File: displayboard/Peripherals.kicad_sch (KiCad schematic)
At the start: 13 parts, among them IC1101 PCAL6416AHF, SW1101 Button 1, SW1102 Button 2, SW1103 Button 3, SW1104 Button 4

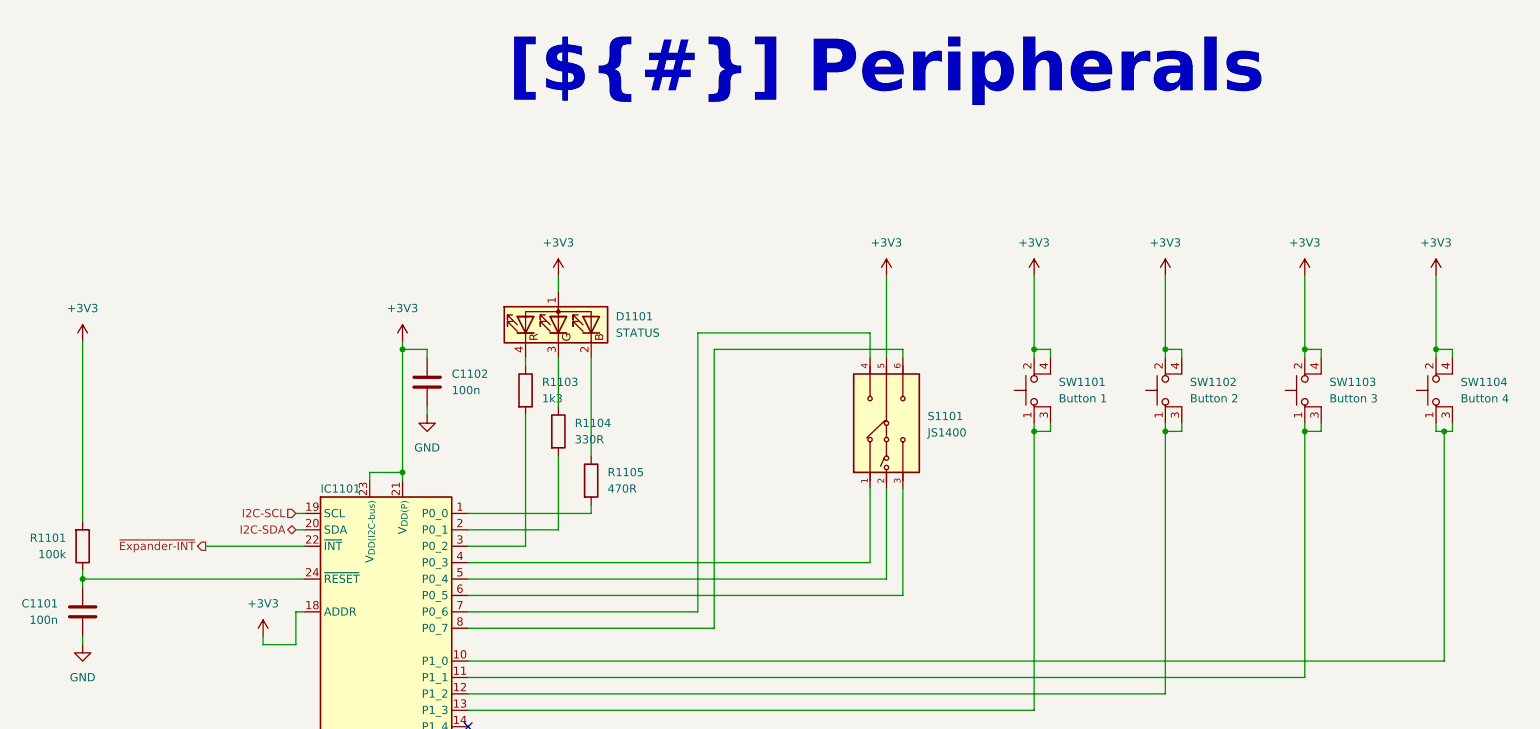
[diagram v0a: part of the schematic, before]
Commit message: Remove old production files, add cutout for the programming cable, add connector for mainboard cable
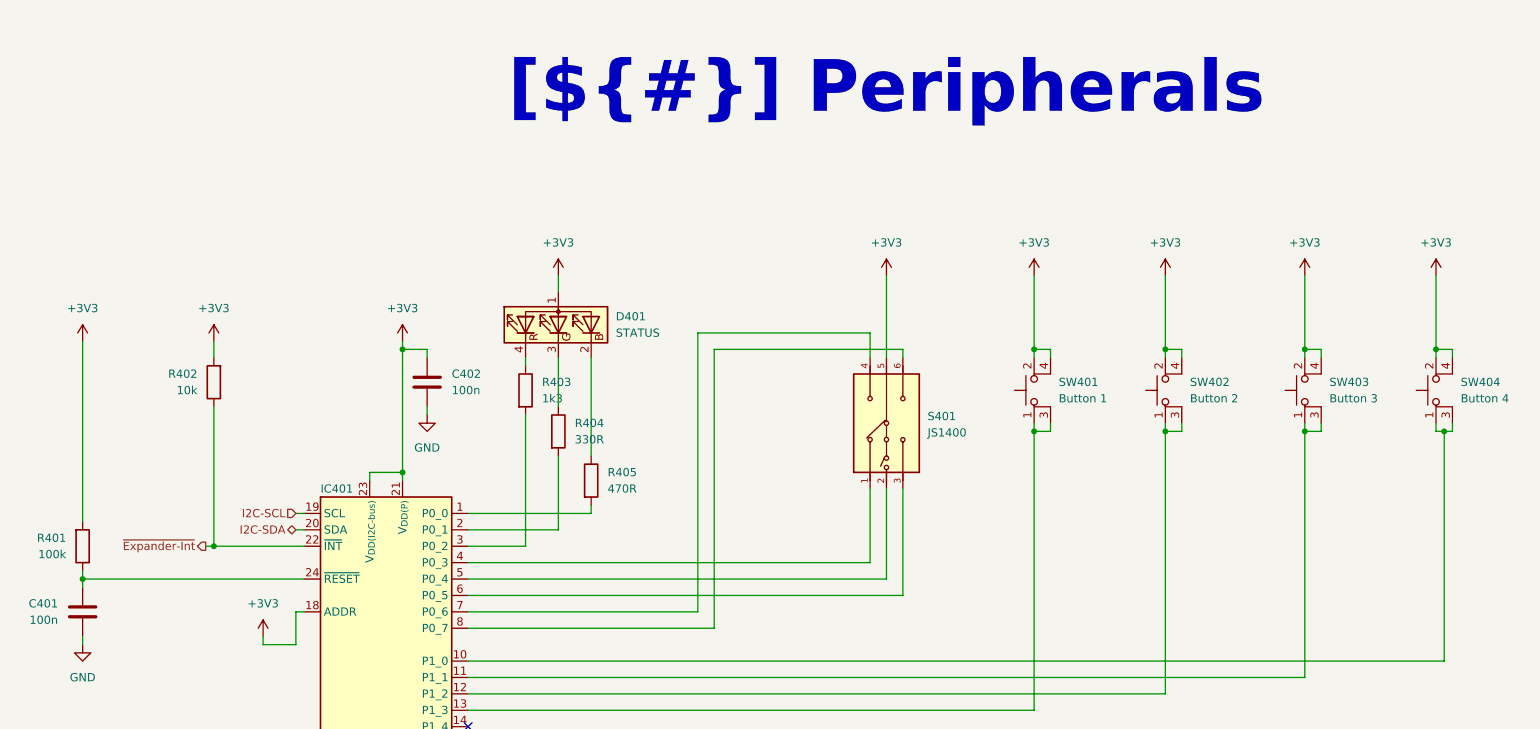
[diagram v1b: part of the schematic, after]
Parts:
- added R402: 10k, Resistor_SMD:R_0805_2012Metric, symbol Device:R
- renumbered C1101 to C401, C1102 to C402, D1101 to D401, IC1101 to IC401, R1101 to R401, R1103 to R403, R1104 to R404, R1105 to R405, S1101 to S401, SW1101 to SW401, SW1102 to SW402, SW1103 to SW403, SW1104 to SW404
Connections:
- net +3V3: now also R402.2
- net ~{Expander-INT} renamed ~{Expander-Int}
- net ~{Expander-Int}: now also R402.1

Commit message: Feature: Issue #19
- Replace JS1400BFQ with MU-BUE70R
- Add CI/CD workflow to check for changelog updates on PRs

Closes #19

Signed-off-by: Daniel Kampert <DanielKampert@kampis-elektroecke.de>
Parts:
- S401: value JS1400 -> NAVIGATION; footprint E-Switch:JS1400BVQ -> Apem:MU-BUE70R; symbol E-Switch:JS1400 -> Apem:MU; manf E-Switch -> Apem; manf# JS1400 -> MU-BUE70R; mouser# 612-JS1400 -> 642-MU-BUE70R
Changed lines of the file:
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@@
 	)
 	(symbol
-		(lib_id "E-Switch:JS1400")
+		(lib_id "Apem:MU")
 		(at 148.59 74.93 90)
 		(unit 1)
@@
 			)
 		)
-		(property "Value" "JS1400"
+		(property "Value" "NAVIGATION"
 			(at 154.94 76.4031 90)
 			(effects
@@
 			)
 		)
-		(property "Footprint" "E-Switch:JS1400BVQ"
+		(property "Footprint" "Apem:MU-BUE70R"
 			(at 235.89 48.26 0)
 			(effects
@@
 			)
 		)
-		(property "Datasheet" "https://configured-product-images.s3.amazonaws.com/2D/specs/JS1400BVQ.pdf"
+		(property "Datasheet" "https://www.apem.com/de/medias/download/PCB_MU_serie.pdf"
 			(at 335.89 48.26 0)
 			(effects
@@
 			)
 		)
-		(property "manf" "E-Switch"
+		(property "manf" "Apem"
 			(at 148.59 74.93 0)
 			(effects
@@
 			)
 		)
-		(property "manf#" "JS1400"
+		(property "manf#" "MU-BUE70R"
 			(at 148.59 74.93 0)
 			(effects
@@
 			)
 		)
-		(property "mouser#" "612-JS1400"
+		(property "mouser#" "642-MU-BUE70R"
 			(at 148.59 74.93 0)
 			(effects

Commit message: Added: Add a cutout for the display cable, add different assembly improvements
Signed-off-by: Daniel Kampert <DanielKampert@kampis-elektroecke.de>
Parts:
- D401: value STATUS -> Status
- S401: value NAVIGATION -> Navigation
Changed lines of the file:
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@@
 			)
 		)
-		(property "Value" "STATUS"
+		(property "Value" "Status"
 			(at 106.68 60.9599 90)
 			(effects
@@
 			)
 		)
-		(property "Value" "NAVIGATION"
+		(property "Value" "Navigation"
 			(at 154.94 76.4031 90)
 			(effects

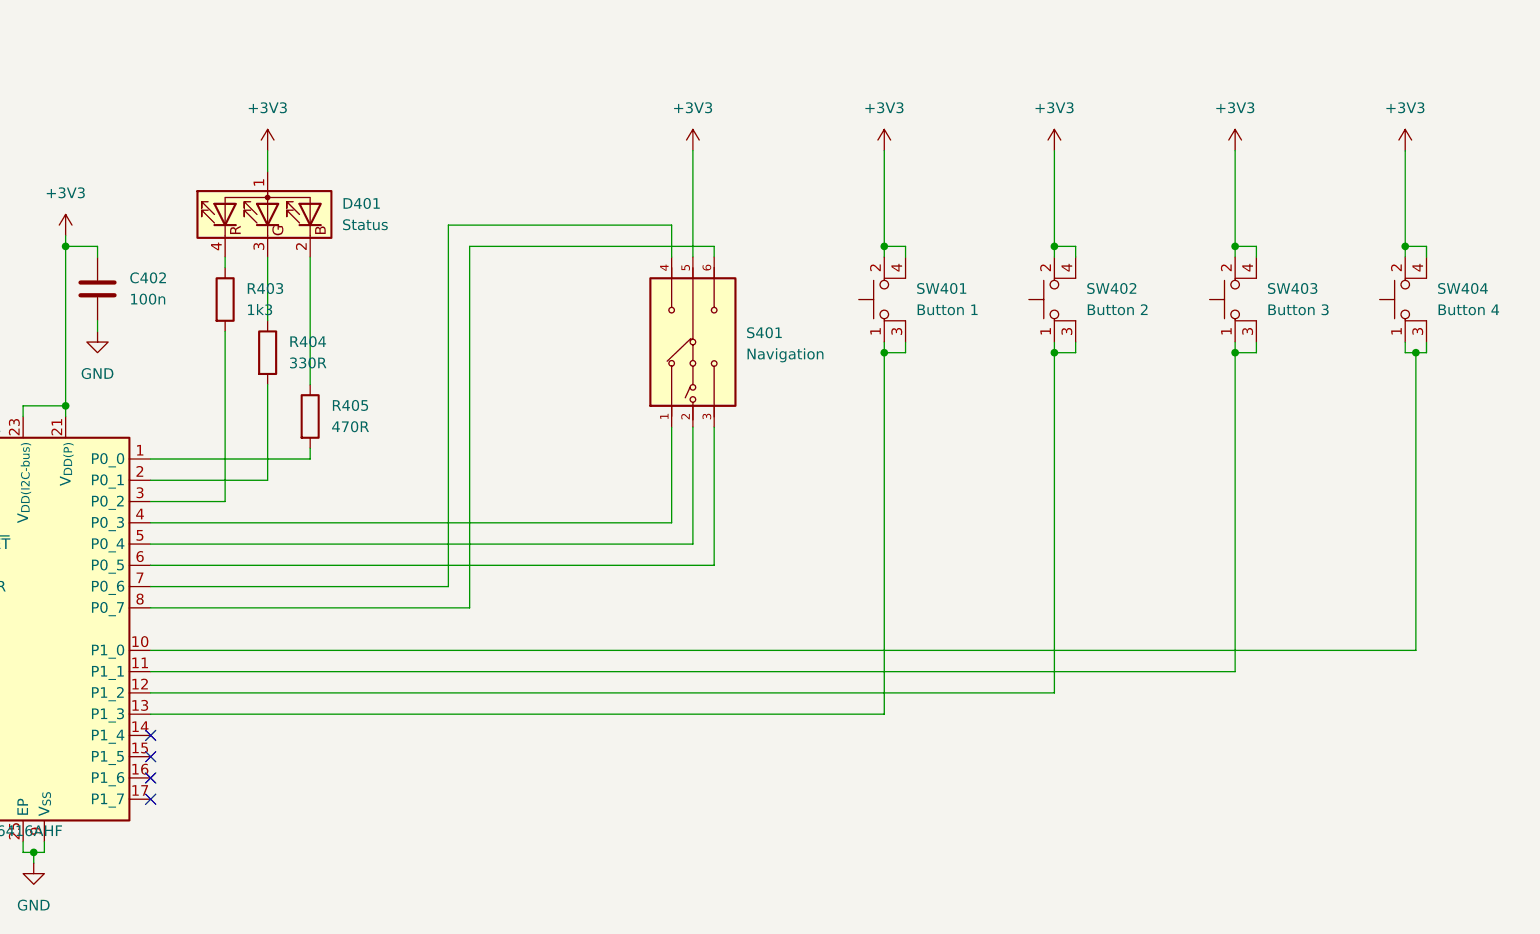
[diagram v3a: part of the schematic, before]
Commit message: Feature: Add debounce capacitors to push buttons
- Replace NPN transistor with N-Channel MOSFET

Signed-off-by: Daniel Kampert <DanielKampert@kampis-elektroecke.de>
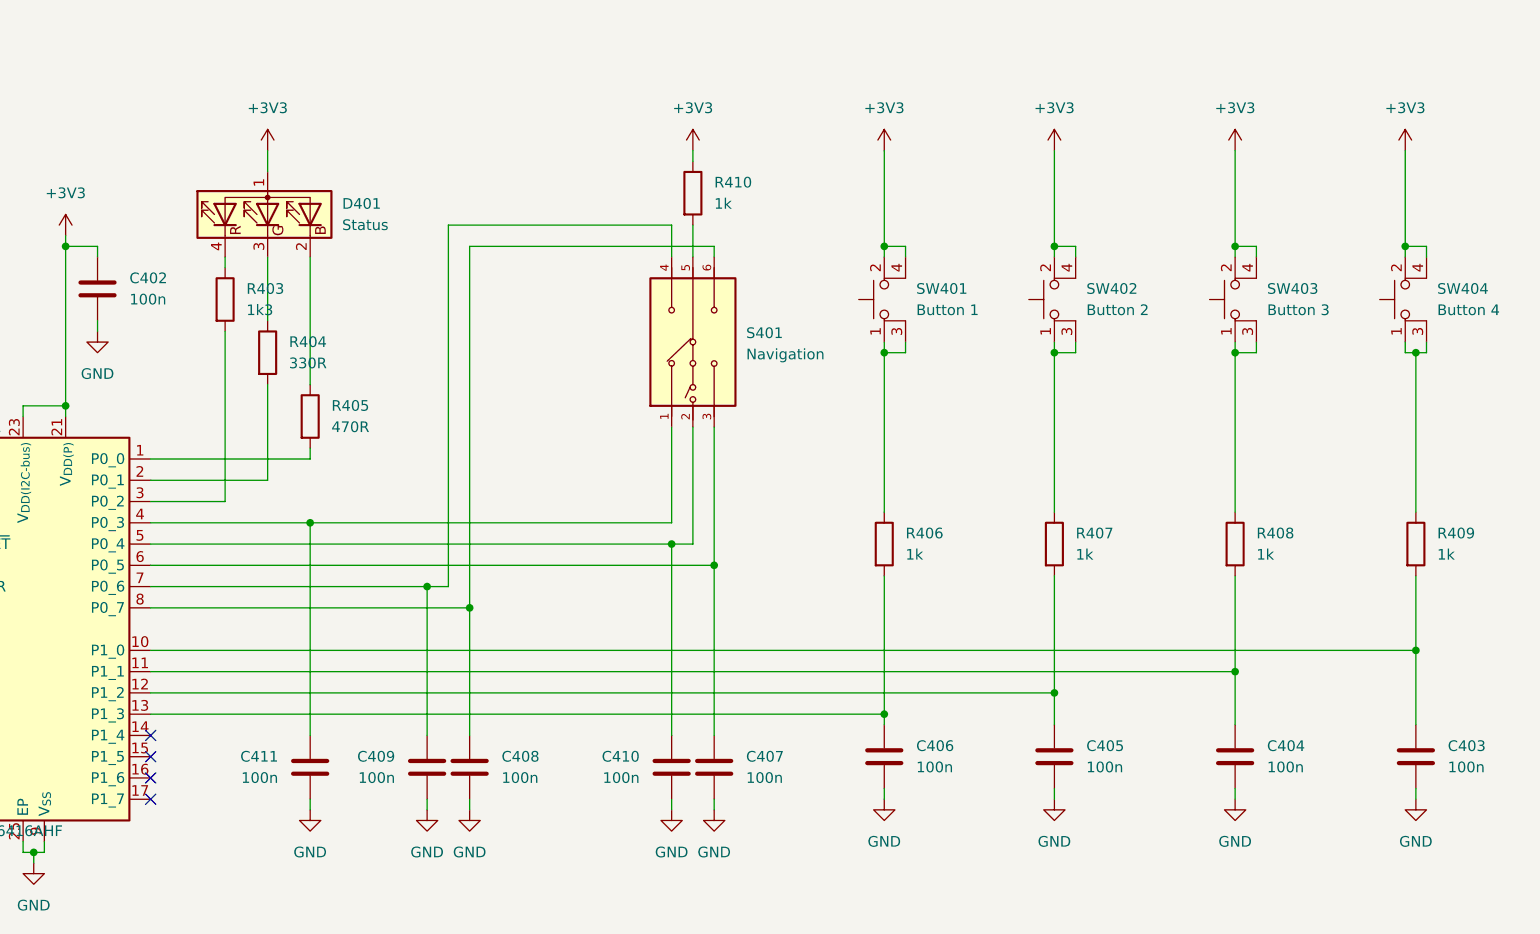
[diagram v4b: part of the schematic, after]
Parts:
- added C403, C404, C405, C406, C407, C408, C409, C410, C411: 100n, Capacitor_SMD:C_0805_2012Metric, symbol Device:C
- added R406, R407, R408, R409, R410: 1k, Resistor_SMD:R_0805_2012Metric, symbol Device:R
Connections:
- net +3V3: now also R410.1; no longer S401.5
- net GND: now also C403.2, C404.2, C405.2, C406.2, C407.2, C408.2, C409.2, C410.2, C411.2
- net at SW401.1, SW401.3: now also R406.1; no longer IC401.13 (P1_3)
- net at SW403.1, SW403.3: now also R408.1; no longer IC401.11 (P1_1)
- net at SW402.1, SW402.3: now also R407.1; no longer IC401.12 (P1_2)
- net at SW404.1, SW404.3: now also R409.1; no longer IC401.10 (P1_0)
- net at IC401.4 (P0_3), S401.1: now also C411.1
- net at IC401.5 (P0_4), S401.2: now also C410.1
- net at IC401.6 (P0_5), S401.3: now also C407.1
- net at IC401.7 (P0_6), S401.4: now also C409.1
- net at IC401.8 (P0_7), S401.6: now also C408.1
- new net: C406.1, IC401.13 (P1_3), R406.2
- new net: C403.1, IC401.10 (P1_0), R409.2
- new net: C405.1, IC401.12 (P1_2), R407.2
- new net: C404.1, IC401.11 (P1_1), R408.2
- new net: R410.2, S401.5

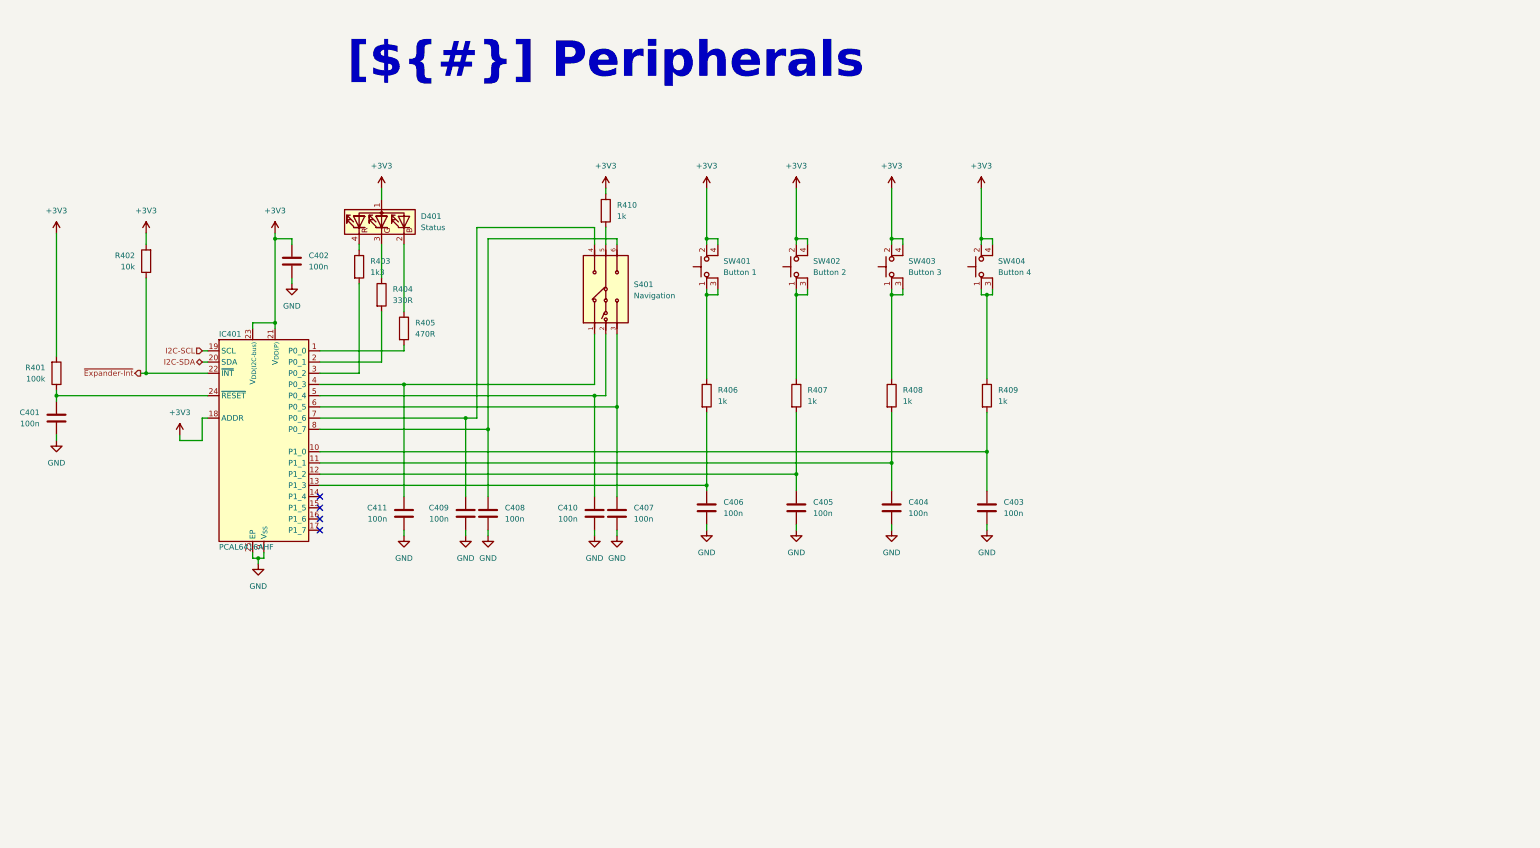
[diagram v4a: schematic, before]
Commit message: Changed: Rework debouncing logic
Signed-off-by: Daniel Kampert <DanielKampert@kampis-elektroecke.de>
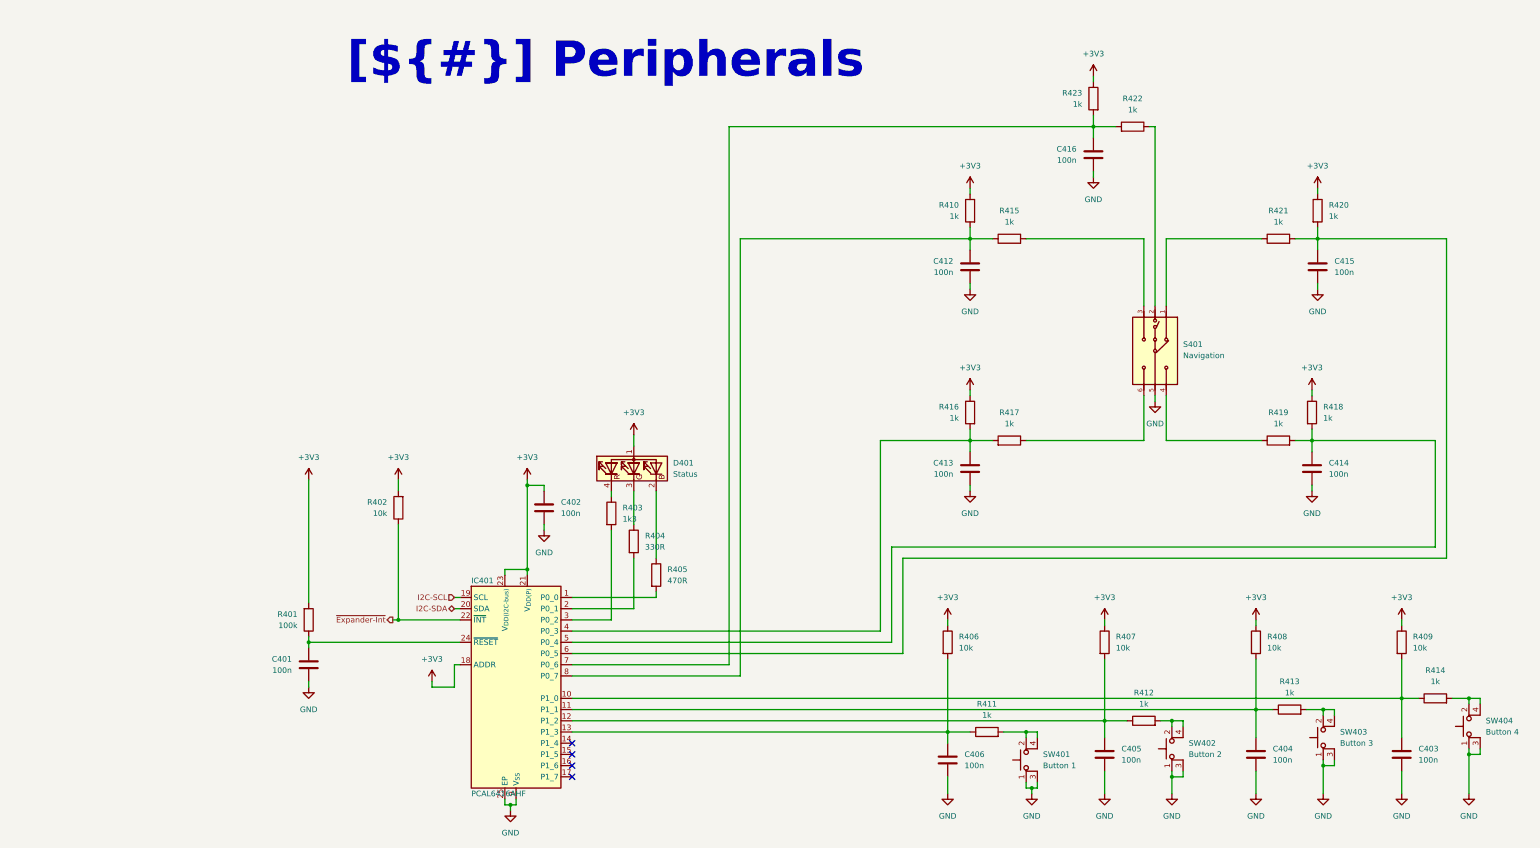
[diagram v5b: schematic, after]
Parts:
- removed C407, C408, C409, C410, C411: 100n, Capacitor_SMD:C_0805_2012Metric, symbol Device:C
- added C412, C413, C414, C415, C416: 100n, Capacitor_SMD:C_0805_2012Metric, symbol Device:C
- added R411, R412, R413, R414, R415, R416, R417, R418, R419, R420, R421, R422, R423: 1k, Resistor_SMD:R_0805_2012Metric, symbol Device:R
- R406: value 1k -> 10k; manf# CR0805-JW-102ELF -> CR0805-JW-103ELF; mouser# 652-CR0805JW-102ELF -> 652-CR0805JW-103ELF
- R407, R408, R409: value 1k -> 10k; manf# CR0805-JW-102ELF -> CR0805-JW-103ELF; mouser# 652-CR0805JW-102ELF -> 652-CR0805-JW-103ELF
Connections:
- net +3V3: now also R406.1, R407.1, R408.1, R409.1, R416.1, R418.1, R420.1, R423.1; no longer SW401.2, SW401.4, SW402.2, SW402.4, SW403.2, SW403.4, SW404.2, SW404.4
- net GND: now also S401.5, SW401.1, SW401.3, SW402.1, SW402.3, SW403.1, SW403.3, SW404.1, SW404.3, C412.2, C413.2, C414.2, C415.2, C416.2
- net at IC401.6 (P0_5): now also C415.1, R420.2, R421.2; no longer S401.3
- net at S401.2: now also R422.1; no longer IC401.5 (P0_4)
- net at C406.1, IC401.13 (P1_3), R406.2: now also R411.1
- net at C403.1, IC401.10 (P1_0), R409.2: now also R414.1
- net at C405.1, IC401.12 (P1_2), R407.2: now also R412.1
- net at IC401.8 (P0_7): now also R410.2, C412.1, R415.1; no longer S401.6
- net at IC401.7 (P0_6): now also C416.1, R422.2, R423.2; no longer S401.4
- net at C404.1, IC401.11 (P1_1), R408.2: now also R413.1
- net at IC401.4 (P0_3): now also C413.1, R416.2, R417.2; no longer S401.1
- new net: R414.2, SW404.2, SW404.4
- new net: R411.2, SW401.2, SW401.4
- new net: R413.2, SW403.2, SW403.4
- new net: R412.2, SW402.2, SW402.4
- new net: R421.1, S401.1
- new net: R419.1, S401.4
- new net: C414.1, IC401.5 (P0_4), R418.2, R419.2
- new net: R417.1, S401.6
- new net: R415.2, S401.3
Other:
- moved on the sheet: C401, C402, C403, C404, C405, C406, D401, IC401, R401, R402, R403, R404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
